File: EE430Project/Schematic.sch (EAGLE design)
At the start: 10 parts, among them T1 2N2222

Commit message: Hi Paco
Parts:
- added SV1: (no value), con-lstb:MA04-1
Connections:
- net N$6 renamed VCC
- net N$7 renamed GND
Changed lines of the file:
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@@
 <layers>
 <layer number="1" name="Top" color="4" fill="1" visible="no" active="no"/>
+<layer number="2" name="Route2" color="1" fill="3" visible="no" active="no"/>
+<layer number="3" name="Route3" color="4" fill="3" visible="no" active="no"/>
+<layer number="4" name="Route4" color="1" fill="4" visible="no" active="no"/>
+<layer number="5" name="Route5" color="4" fill="4" visible="no" active="no"/>
+<layer number="6" name="Route6" color="1" fill="8" visible="no" active="no"/>
+<layer number="7" name="Route7" color="4" fill="8" visible="no" active="no"/>
+<layer number="8" name="Route8" color="1" fill="2" visible="no" active="no"/>
+<layer number="9" name="Route9" color="4" fill="2" visible="no" active="no"/>
+<layer number="10" name="Route10" color="1" fill="7" visible="no" active="no"/>
+<layer number="11" name="Route11" color="4" fill="7" visible="no" active="no"/>
+<layer number="12" name="Route12" color="1" fill="5" visible="no" active="no"/>
+<layer number="13" name="Route13" color="4" fill="5" visible="no" active="no"/>
+<layer number="14" name="Route14" color="1" fill="6" visible="no" active="no"/>
+<layer number="15" name="Route15" color="4" fill="6" visible="no" active="no"/>
 <layer number="16" name="Bottom" color="1" fill="1" visible="no" active="no"/>
 <layer number="17" name="Pads" color="2" fill="1" visible="no" active="no"/>
@@
 <part name="C3" library="capacitor-wima" library_urn="urn:adsk.eagle:library:116" deviceset="C" device="2,5-3" package3d_urn="urn:adsk.eagle:package:5436/1" value=".5uf"/>
 <part name="RL" library="resistor-shunt" library_urn="urn:adsk.eagle:library:346" deviceset="BVS" device="" package3d_urn="urn:adsk.eagle:package:25212/1" value="3.3k"/>
+<part name="SV1" library="con-lstb" library_urn="urn:adsk.eagle:library:162" deviceset="MA04-1" device="" package3d_urn="urn:adsk.eagle:package:8337/1"/>
+<part name="P+1" library="supply1" library_urn="urn:adsk.eagle:library:371" deviceset="VCC" device="">
+<attribute name="VCC" value="15V"/>
+</part>
+<part name="GND1" library="supply1" library_urn="urn:adsk.eagle:library:371" deviceset="GND" device=""/>
 </parts>
 <sheets>
@@
 <attribute name="VALUE" x="74.041" y="59.69" size="1.778" layer="96" rot="R90"/>
 </instance>
+<instance part="SV1" gate="1" x="-17.78" y="101.6" smashed="yes">
+<attribute name="VALUE" x="-19.05" y="91.44" size="1.778" layer="96"/>
+<attribute name="NAME" x="-19.05" y="107.442" size="1.778" layer="95"/>
+</instance>
+<instance part="P+1" gate="VCC" x="38.1" y="101.6" smashed="yes">
+<attribute name="VALUE" x="35.56" y="99.06" size="1.778" layer="96" rot="R90"/>
+<attribute name="VCC" x="38.1" y="101.6" size="1.778" layer="96"/>
+</instance>
+<instance part="GND1" gate="1" x="40.64" y="40.64" smashed="yes">
+<attribute name="VALUE" x="38.1" y="38.1" size="1.778" layer="96"/>
+</instance>
 </instances>
 <busses>
@@
 </segment>
 </net>
-<net name="N$6" class="0">
+<net name="N$5" class="0">
+<segment>
+<pinref part="C3" gate="G$1" pin="2"/>
+<wire x1="60.96" y1="78.74" x2="71.12" y2="78.74" width="0.1524" layer="91"/>
+<pinref part="RL" gate="G$1" pin="1"/>
+<wire x1="71.12" y1="78.74" x2="71.12" y2="68.58" width="0.1524" layer="91"/>
+<wire x1="71.12" y1="78.74" x2="83.82" y2="78.74" width="0.1524" layer="91"/>
+</segment>
+</net>
+<net name="N$8" class="0">
+<segment>
+<pinref part="RS" gate="G$1" pin="2"/>
+<wire x1="-7.62" y1="68.58" x2="-12.7" y2="68.58" width="0.1524" layer="91"/>
+</segment>
+</net>
+<net name="VCC" class="0">
 <segment>
 <pinref part="R1" gate="G$1" pin="1"/>
@@
 <wire x1="43.18" y1="91.44" x2="43.18" y2="88.9" width="0.1524" layer="91"/>
 <wire x1="38.1" y1="91.44" x2="38.1" y2="99.06" width="0.1524" layer="91"/>
-</segment>
-</net>
-<net name="N$7" class="0">
+<pinref part="P+1" gate="VCC" pin="VCC"/>
+</segment>
+</net>
+<net name="GND" class="0">
 <segment>
 <pinref part="C2" gate="G$1" pin="2"/>
@@
 <wire x1="71.12" y1="58.42" x2="71.12" y2="45.72" width="0.1524" layer="91"/>
 <wire x1="71.12" y1="45.72" x2="55.88" y2="45.72" width="0.1524" layer="91"/>
-<wire x1="40.64" y1="45.72" x2="40.64" y2="40.64" width="0.1524" layer="91"/>
+<wire x1="40.64" y1="45.72" x2="40.64" y2="43.18" width="0.1524" layer="91"/>
+<wire x1="40.64" y1="43.18" x2="40.64" y2="40.64" width="0.1524" layer="91"/>
 <wire x1="71.12" y1="45.72" x2="86.36" y2="45.72" width="0.1524" layer="91"/>
-</segment>
-</net>
-<net name="N$5" class="0">
-<segment>
-<pinref part="C3" gate="G$1" pin="2"/>
-<wire x1="60.96" y1="78.74" x2="71.12" y2="78.74" width="0.1524" layer="91"/>
-<pinref part="RL" gate="G$1" pin="1"/>
-<wire x1="71.12" y1="78.74" x2="71.12" y2="68.58" width="0.1524" layer="91"/>
-<wire x1="71.12" y1="78.74" x2="83.82" y2="78.74" width="0.1524" layer="91"/>
-</segment>
-</net>
-<net name="N$8" class="0">
-<segment>
-<pinref part="RS" gate="G$1" pin="2"/>
-<wire x1="-7.62" y1="68.58" x2="-12.7" y2="68.58" width="0.1524" layer="91"/>
-</segment>
-</net>
+<pinref part="GND1" gate="1" pin="GND"/>
+<junction x="40.64" y="43.18"/>
+</segment>
+</net>

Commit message: Hi
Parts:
- removed SV1: (no value), con-lstb:MA04-1
- added J1: (no value), SparkFun-Connectors:QWIIC_CONNECTORJS-1MM
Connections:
- net GND: now also J1.1

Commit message: Hey
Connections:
- removed net N$8: RS.2
- new net VIN: J1.3, RS.2
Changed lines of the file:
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@@
-</segment>
-</net>
-<net name="N$8" class="0">
-<segment>
-<pinref part="RS" gate="G$1" pin="2"/>
-<wire x1="-7.62" y1="68.58" x2="-12.7" y2="68.58" width="0.1524" layer="91"/>
 </segment>
 </net>
@@
 </segment>
 </net>
+<net name="VIN" class="0">
+<segment>
+<pinref part="J1" gate="G$1" pin="3"/>
+<wire x1="-5.08" y1="101.6" x2="7.62" y2="101.6" width="0.1524" layer="91"/>
+<label x="7.62" y="101.6" size="1.778" layer="95" xref="yes"/>
+</segment>
+<segment>
+<pinref part="RS" gate="G$1" pin="2"/>
+<wire x1="-7.62" y1="68.58" x2="-15.24" y2="68.58" width="0.1524" layer="91"/>
+<wire x1="-15.24" y1="76.2" x2="-15.24" y2="68.58" width="0.1524" layer="91"/>
+<label x="-7.62" y="68.58" size="1.778" layer="95" rot="R180" xref="yes"/>
+</segment>
+</net>

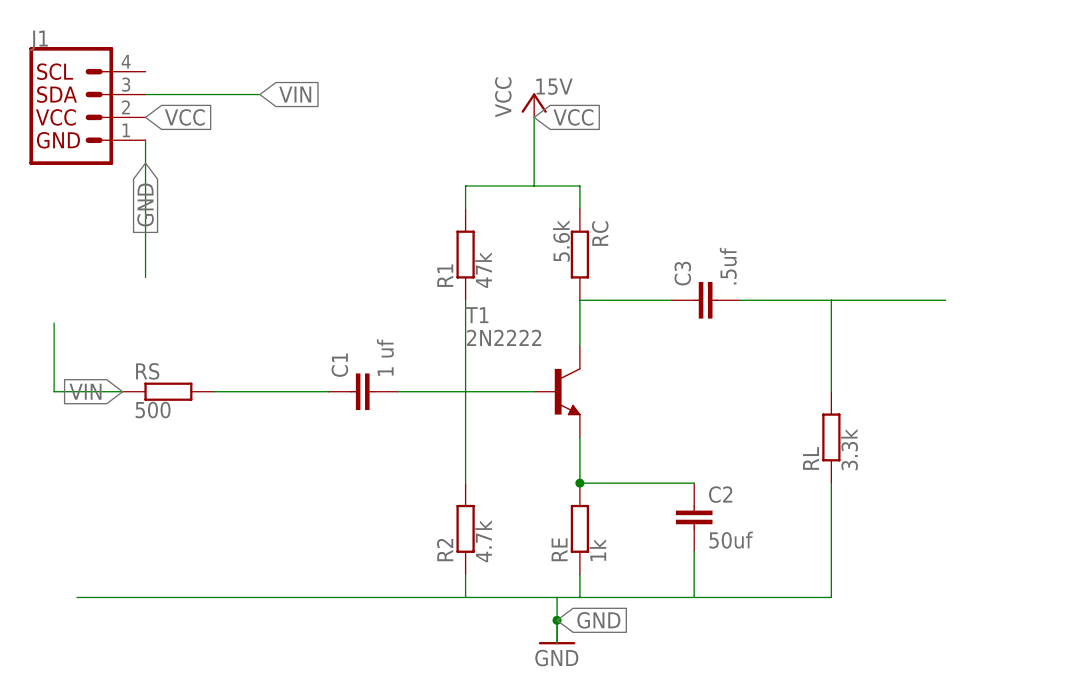
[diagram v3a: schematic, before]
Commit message: Just added the output label, i think we are ready to do rats nest next
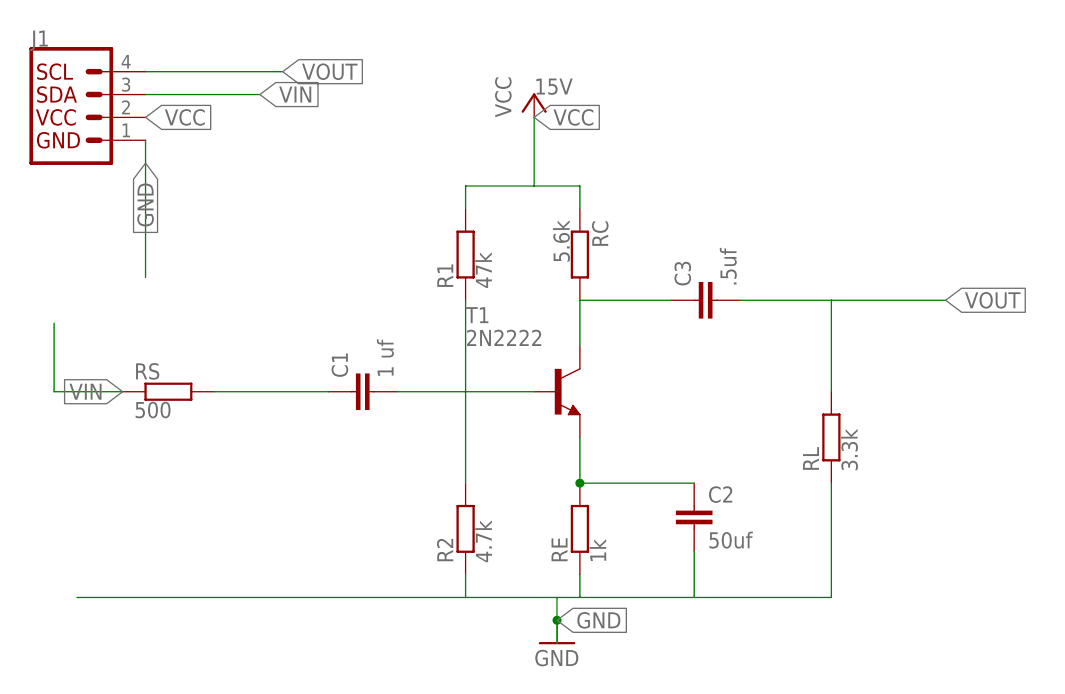
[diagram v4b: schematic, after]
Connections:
- removed net N$5: C3.2, RL.1
- new net VOUT: C3.2, J1.4, RL.1
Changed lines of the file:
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@@
 </segment>
 </net>
-<net name="N$5" class="0">
+<net name="VOUT" class="0">
 <segment>
 <pinref part="C3" gate="G$1" pin="2"/>
@@
 <wire x1="71.12" y1="78.74" x2="71.12" y2="68.58" width="0.1524" layer="91"/>
 <wire x1="71.12" y1="78.74" x2="83.82" y2="78.74" width="0.1524" layer="91"/>
+<label x="83.82" y="78.74" size="1.778" layer="95" xref="yes"/>
+</segment>
+<segment>
+<pinref part="J1" gate="G$1" pin="4"/>
+<wire x1="-5.08" y1="104.14" x2="10.16" y2="104.14" width="0.1524" layer="91"/>
+<label x="10.16" y="104.14" size="1.778" layer="95" xref="yes"/>
 </segment>
 </net>
